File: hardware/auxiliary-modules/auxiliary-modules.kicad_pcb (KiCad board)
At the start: 2 copper layers, 40.5 x 74.5 mm, 36 parts, among them J1 IDC-10, J2 Conn_01x07, J3 Conn_01x04, J4 IDC-10, J5 IDC-10, U1 CS49E, U2 NTS0102, U3 LM393, U4 NTS0102

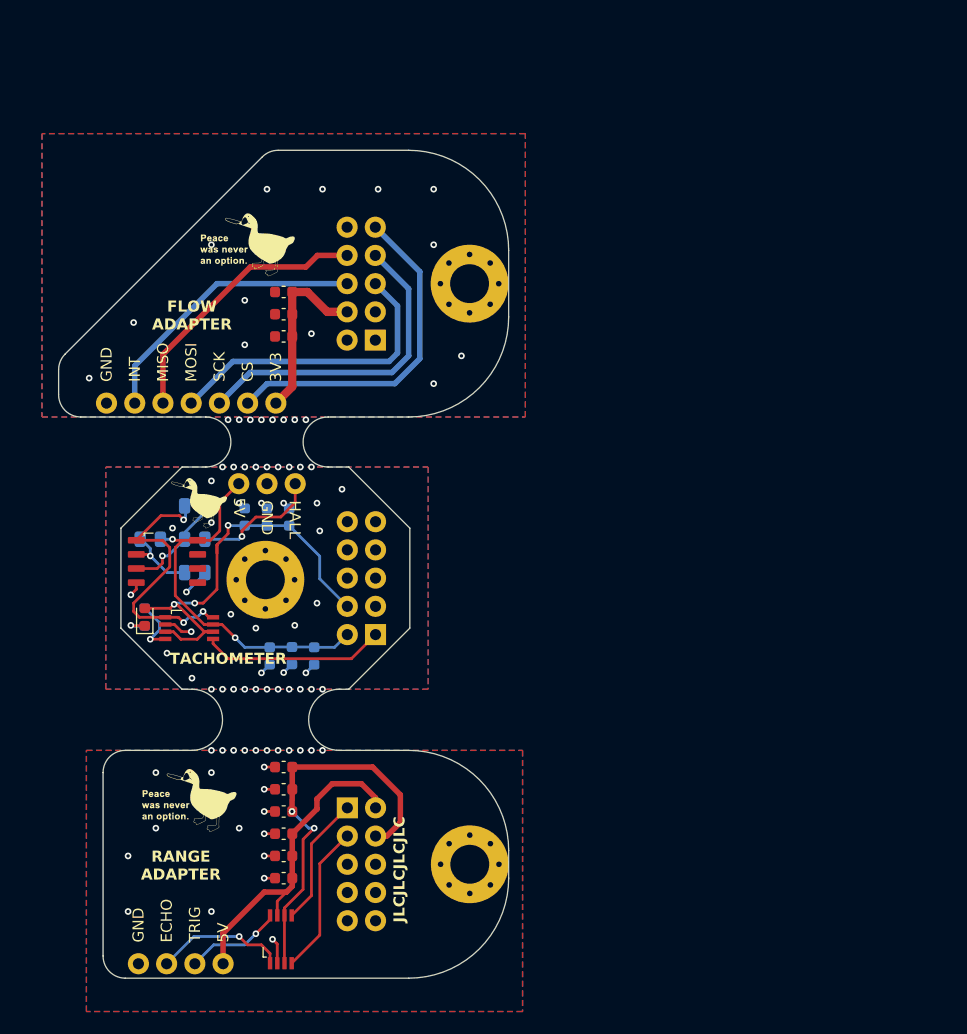
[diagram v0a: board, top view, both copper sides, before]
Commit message: routing: AUX panel fix
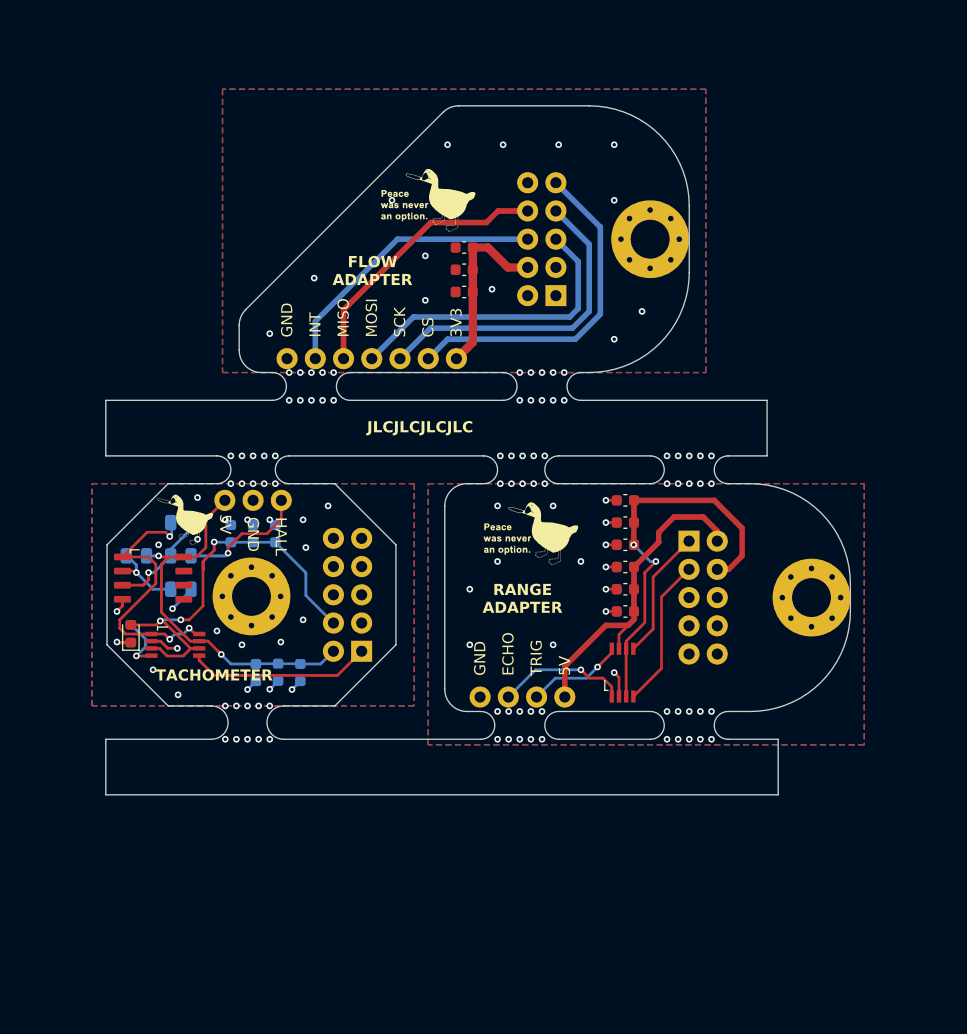
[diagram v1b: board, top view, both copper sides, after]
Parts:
- moved C10 39.0 mm to (182.2, 93.0)
- moved C11 39.0 mm to (182.2, 95.0)
- moved C12 39.0 mm to (182.2, 97.0)
- moved C7 39.0 mm to (182.2, 99.0)
- moved C8 39.0 mm to (182.2, 101.0)
- moved C9 39.0 mm to (182.2, 103.0)
- moved G*** 39.0 mm to (173.8, 96.0)
- moved H3 39.0 mm to (199.0, 101.8)
- moved J4 39.0 mm to (189.2, 101.8)
- moved U4 39.0 mm to (182.0, 108.5)
- moved J3 39.0 mm to (176.8, 110.7)
- moved C13 16.7 mm to (167.8, 70.2)
- moved C14 16.7 mm to (167.8, 72.2)
- moved C15 16.7 mm to (167.8, 74.2)
- moved G*** 16.7 mm to (164.5, 66.0)
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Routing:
- net RANGE_GND: vias 24 -> 14
- net TACH_GND: vias 31 -> 21
- net (no net): vias 19 -> 80
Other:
- board size 40.5 x 74.5 mm -> 67 x 62 mm

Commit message: panel V3
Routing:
- net (no net): vias 80 -> 90
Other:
- board size 67 x 62 mm -> 83 x 69.5 mm
